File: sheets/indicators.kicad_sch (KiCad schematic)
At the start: 18 parts, among them Q1 AO3400A

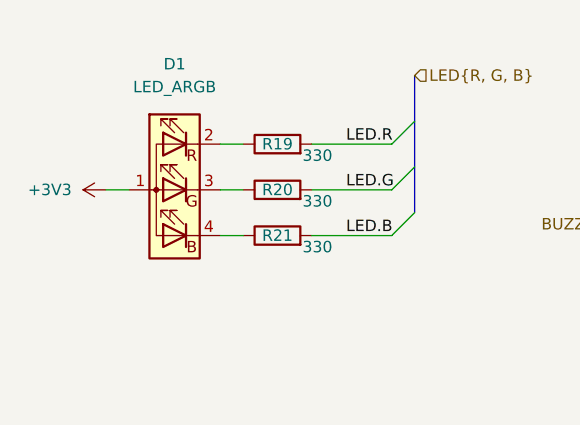
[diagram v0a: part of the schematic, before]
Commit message: solved reverse polarity w pmos and tvs clamp
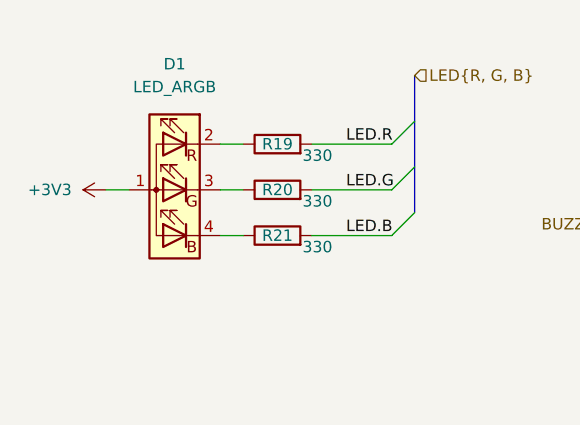
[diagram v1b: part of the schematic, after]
